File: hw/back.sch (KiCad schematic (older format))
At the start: 21 parts, among them J1 IDC_02X13, U1 OSRB38C9BA, U2 MCP1826S

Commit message: updated schematic ERC ok
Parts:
- added C6, C9: 1u, symbol Device:C
- added C7, C8: 100n, symbol Device:C
- added U3: MCP1826S, Package_TO_SOT_SMD:SOT-223-3_TabPin2, symbol Regulator_Linear:MCP1826S
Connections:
- net +5V: now also C6.1, C7.1, U3.1 (VI)
- net GND: now also C6.2, C7.2, C8.2, C9.2, U3.2 (GND)
- new net +3V3: C8.1, C9.1, U3.3 (VO)
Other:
- moved on the sheet: C2, C3, C4, C5, U2

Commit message: updated schematic
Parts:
- H1, H2, H3, H4: value Screw -> M3; symbol KLIB_Mech:Screw -> KLIB_Mechanical:Bolt
- J1: symbol KLIB_Con_IDC:IDC_02X13 -> KLIB_Connector_IDC:IDC_02X13
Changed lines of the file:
@@
 	1400 4000 1100 4000
 $Comp
-L KLIB_Con_IDC:IDC_02X13 J1
+L KLIB_Connector_IDC:IDC_02X13 J1
 U 1 1 5AC4FF09
 P 1700 4200
@@
 Connection ~ 1100 4000
 $Comp
-L KLIB_Mech:Screw H2
+L KLIB_Mechanical:Bolt H2
 U 1 1 5ACAE88A
 P 6600 3950
 F 0 "H2" H 6705 4021 50  0000 L CNN
-F 1 "Screw" H 6705 3930 50  0000 L CNN
+F 1 "M3" H 6705 3930 50  0000 L CNN
 F 2 "wyk_mech:screw_M3" H 6700 3800 50  0001 L CNN
 F 3 "~" H 6725 3875 50  0001 C CNN
@@
 $EndComp
 $Comp
-L KLIB_Mech:Screw H3
+L KLIB_Mechanical:Bolt H3
 U 1 1 5ACAEAD6
 P 7000 3950
 F 0 "H3" H 7105 4021 50  0000 L CNN
-F 1 "Screw" H 7105 3930 50  0000 L CNN
+F 1 "M3" H 7105 3930 50  0000 L CNN
 F 2 "wyk_mech:screw_M3" H 7100 3800 50  0001 L CNN
 F 3 "~" H 7125 3875 50  0001 C CNN
@@
 $EndComp
 $Comp
-L KLIB_Mech:Screw H4
+L KLIB_Mechanical:Bolt H4
 U 1 1 5ACAEB1D
 P 7400 3950
 F 0 "H4" H 7505 4021 50  0000 L CNN
-F 1 "Screw" H 7505 3930 50  0000 L CNN
+F 1 "M3" H 7505 3930 50  0000 L CNN
 F 2 "wyk_mech:screw_M3" H 7500 3800 50  0001 L CNN
 F 3 "~" H 7525 3875 50  0001 C CNN
@@
 $EndComp
 $Comp
-L KLIB_Mech:Screw H1
+L KLIB_Mechanical:Bolt H1
 U 1 1 5ACAEC08
 P 6200 3950
 F 0 "H1" H 6305 4021 50  0000 L CNN
-F 1 "Screw" H 6305 3930 50  0000 L CNN
+F 1 "M3" H 6305 3930 50  0000 L CNN
 F 2 "wyk_mech:screw_M3" H 6300 3800 50  0001 L CNN
 F 3 "~" H 6325 3875 50  0001 C CNN

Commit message: updated schematic
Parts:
- C1: footprint (none) -> Capacitor_Tantalum_SMD:CP_EIA-7343-31_Kemet-D
- C2, C5, C6, C9: value 1u -> 1u/50V; footprint (none) -> Capacitor_SMD:C_0805_2012Metric
- C3, C4, C7, C8: footprint (none) -> Capacitor_SMD:C_0805_2012Metric
- D1, D2: footprint LEDs:LED_WS2812-PLCC6 -> KLIB_Opto:LED_RGB_5050-6
- J1: footprint Connectors:IDC_Header_Straight_26pins -> Connector_IDC:IDC-Header_2x13_P2.54mm_Vertical
- R1, R2, R3, R4, R5, R6, R7: footprint (none) -> Resistor_SMD:R_0805_2012Metric
- U1: footprint (none) -> KLIB_Opto:OSRB8C9BA_Horizontal
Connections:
- net GND: now also J1.12, J1.14, J1.16, J1.18, J1.20, J1.22, J1.24, J1.26; no longer J1.11, J1.13, J1.15, J1.17, J1.19, J1.21, J1.23, J1.25
- net IR_Rx: now also J1.25; no longer J1.26
- net PWM_B: now also J1.15; no longer J1.16
- net PWM_G: now also J1.13; no longer J1.14
- net PWM_R: now also J1.11; no longer J1.12
- net SCL: now also J1.19; no longer J1.20
- net SDA: now also J1.17; no longer J1.18
- net ~AL: now also J1.23; no longer J1.24
- net ~INT: now also J1.21; no longer J1.22
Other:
- moved on the sheet: C2, C3, C4, C5, C6, C7, C8, C9, J1, U2, U3

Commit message: updated schematic
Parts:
- H1, H2, H3, H4: footprint wyk_mech:screw_M3 -> KLIB_Mechanical:Bolt_M3
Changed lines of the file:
@@
 	2250 3800 2250 3850
-$Comp
-L KLIB_Mechanical:Bolt H2
-U 1 1 5ACAE88A
-P 6600 3950
-F 0 "H2" H 6705 4021 50  0000 L CNN
-F 1 "M3" H 6705 3930 50  0000 L CNN
-F 2 "wyk_mech:screw_M3" H 6700 3800 50  0001 L CNN
-F 3 "~" H 6725 3875 50  0001 C CNN
-	1    6600 3950
-	1    0    0    -1
-$EndComp
-$Comp
-L KLIB_Mechanical:Bolt H3
-U 1 1 5ACAEAD6
-P 7000 3950
-F 0 "H3" H 7105 4021 50  0000 L CNN
-F 1 "M3" H 7105 3930 50  0000 L CNN
-F 2 "wyk_mech:screw_M3" H 7100 3800 50  0001 L CNN
-F 3 "~" H 7125 3875 50  0001 C CNN
-	1    7000 3950
-	1    0    0    -1
-$EndComp
-$Comp
-L KLIB_Mechanical:Bolt H4
-U 1 1 5ACAEB1D
-P 7400 3950
-F 0 "H4" H 7505 4021 50  0000 L CNN
-F 1 "M3" H 7505 3930 50  0000 L CNN
-F 2 "wyk_mech:screw_M3" H 7500 3800 50  0001 L CNN
-F 3 "~" H 7525 3875 50  0001 C CNN
-	1    7400 3950
-	1    0    0    -1
-$EndComp
-$Comp
-L KLIB_Mechanical:Bolt H1
-U 1 1 5ACAEC08
-P 6200 3950
-F 0 "H1" H 6305 4021 50  0000 L CNN
-F 1 "M3" H 6305 3930 50  0000 L CNN
-F 2 "wyk_mech:screw_M3" H 6300 3800 50  0001 L CNN
-F 3 "~" H 6325 3875 50  0001 C CNN
-	1    6200 3950
-	1    0    0    -1
-$EndComp
 $Comp
 L KLIB_Power:PWR_FLAG #FLG02
@@
 	1    0    0    -1
 $EndComp
+$Comp
+L KLIB_Mechanical:Bolt H1
+U 1 1 5AFB06E8
+P 6000 3900
+F 0 "H1" H 6105 3971 50  0000 L CNN
+F 1 "M3" H 6105 3880 50  0000 L CNN
+F 2 "KLIB_Mechanical:Bolt_M3" H 6100 3750 50  0001 L CNN
+F 3 "~" H 6125 3825 50  0001 C CNN
+	1    6000 3900
+	1    0    0    -1
+$EndComp
+$Comp
+L KLIB_Mechanical:Bolt H2
+U 1 1 5AFB0770
+P 6400 3900
+F 0 "H2" H 6505 3971 50  0000 L CNN
+F 1 "M3" H 6505 3880 50  0000 L CNN
+F 2 "KLIB_Mechanical:Bolt_M3" H 6500 3750 50  0001 L CNN
+F 3 "~" H 6525 3825 50  0001 C CNN
+	1    6400 3900
+	1    0    0    -1
+$EndComp
+$Comp
+L KLIB_Mechanical:Bolt H3
+U 1 1 5AFB07B1
+P 6800 3900
+F 0 "H3" H 6905 3971 50  0000 L CNN
+F 1 "M3" H 6905 3880 50  0000 L CNN
+F 2 "KLIB_Mechanical:Bolt_M3" H 6900 3750 50  0001 L CNN
+F 3 "~" H 6925 3825 50  0001 C CNN
+	1    6800 3900
+	1    0    0    -1
+$EndComp
+$Comp
+L KLIB_Mechanical:Bolt H4
+U 1 1 5AFB07FC
+P 7200 3900
+F 0 "H4" H 7305 3971 50  0000 L CNN
+F 1 "M3" H 7305 3880 50  0000 L CNN
+F 2 "KLIB_Mechanical:Bolt_M3" H 7300 3750 50  0001 L CNN
+F 3 "~" H 7325 3825 50  0001 C CNN
+	1    7200 3900
+	1    0    0    -1
+$EndComp

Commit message: updated schematic
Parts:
- added D3, D4: LTST-G563ZEGBW, KLIB_Opto:LED_RGB_5050-6, symbol KLIB_Opto:LTST-G563ZEGBW
- added R10, R13: 180R, Resistor_SMD:R_0805_2012Metric, symbol Device:R
- added R11, R12, R8, R9: 120R, Resistor_SMD:R_0805_2012Metric, symbol Device:R
- renumbered C2 to C1, C1 to C2, R2 to R1, R3 to R2, R4 to R3, R5 to R4, R6 to R5, R7 to R6, R1 to R7
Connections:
- net +5V: now also D3.4 (BA), D3.5 (GA), D3.6 (RA), D4.4 (BA), D4.5 (GA), D4.6 (RA)
- net PWM_B: now also R11.2, R8.2
- net PWM_G: now also R12.2, R9.2
- net PWM_R: now also R10.2, R13.2
- new net: D3.2 (GK), R9.1
- new net: D3.3 (BK), R10.1
- new net: D3.1 (RK), R8.1
- new net: D4.2 (GK), R12.1
- new net: D4.3 (BK), R13.1
- new net: D4.1 (RK), R11.1
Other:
- moved on the sheet: C1, C2, C3, C4, C5, C6, C7, C8, C9, D1, D2, H1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

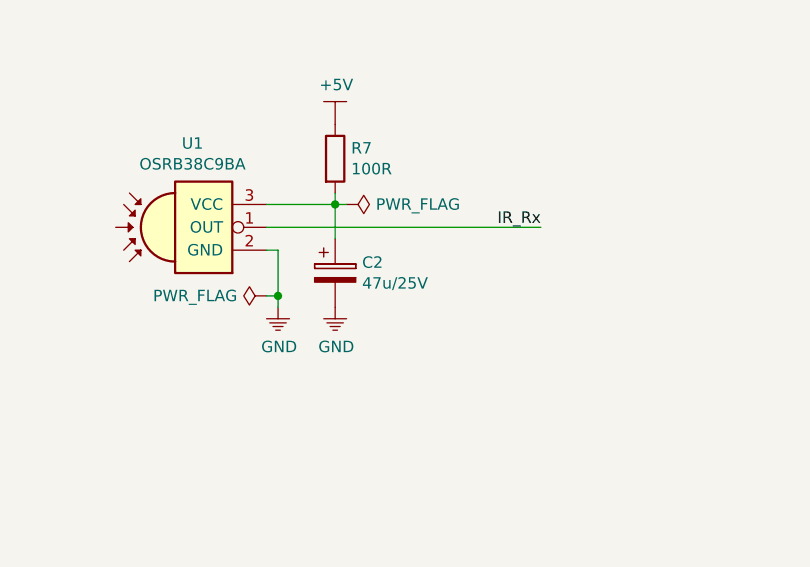
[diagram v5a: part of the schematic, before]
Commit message: updated C2 footprint
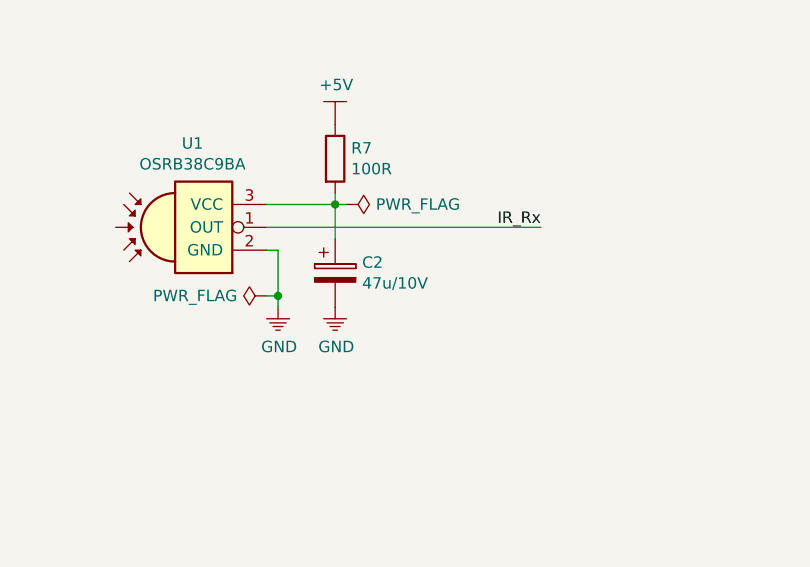
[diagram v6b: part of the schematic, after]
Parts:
- C2: value 47u/25V -> 47u/10V; footprint Capacitor_Tantalum_SMD:CP_EIA-7343-31_Kemet-D -> Capacitor_Tantalum_SMD:CP_EIA-3528-21_Kemet-B
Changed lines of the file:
@@
 P 5300 6400
 F 0 "C2" H 5418 6446 50  0000 L CNN
-F 1 "47u/25V" H 5418 6355 50  0000 L CNN
-F 2 "Capacitor_Tantalum_SMD:CP_EIA-7343-31_Kemet-D" H 5338 6250 50  0001 C CNN
+F 1 "47u/10V" H 5418 6355 50  0000 L CNN
+F 2 "Capacitor_Tantalum_SMD:CP_EIA-3528-21_Kemet-B" H 5338 6250 50  0001 C CNN
 F 3 "~" H 5300 6400 50  0001 C CNN
 	1    5300 6400
